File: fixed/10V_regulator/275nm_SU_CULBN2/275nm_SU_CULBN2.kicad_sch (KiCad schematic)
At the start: 18 parts, among them J1 Conn_01x04, J2 Conn_01x04, Q1 MMBT5551L, U2 LMV321, U3 AP3012

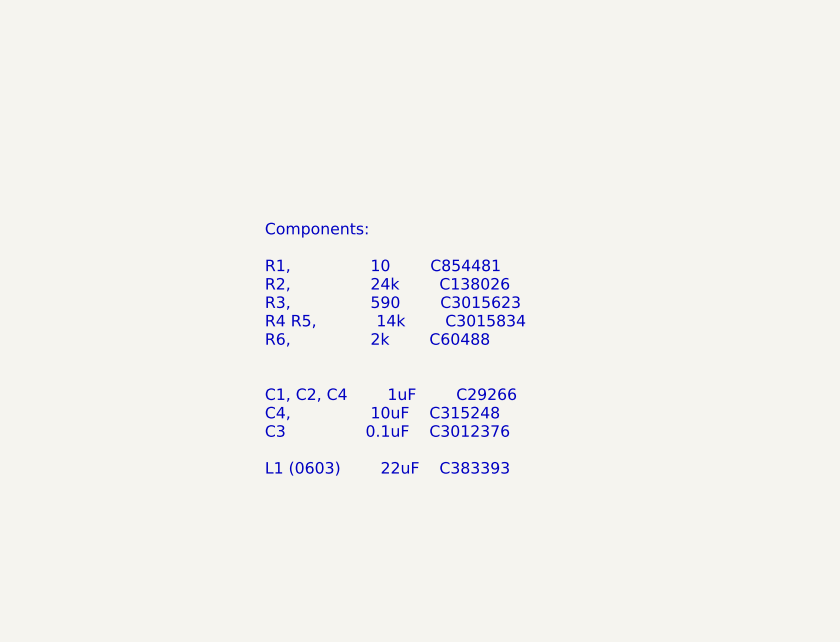
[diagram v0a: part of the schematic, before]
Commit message: Finished component selection for fixed 275nm LED.
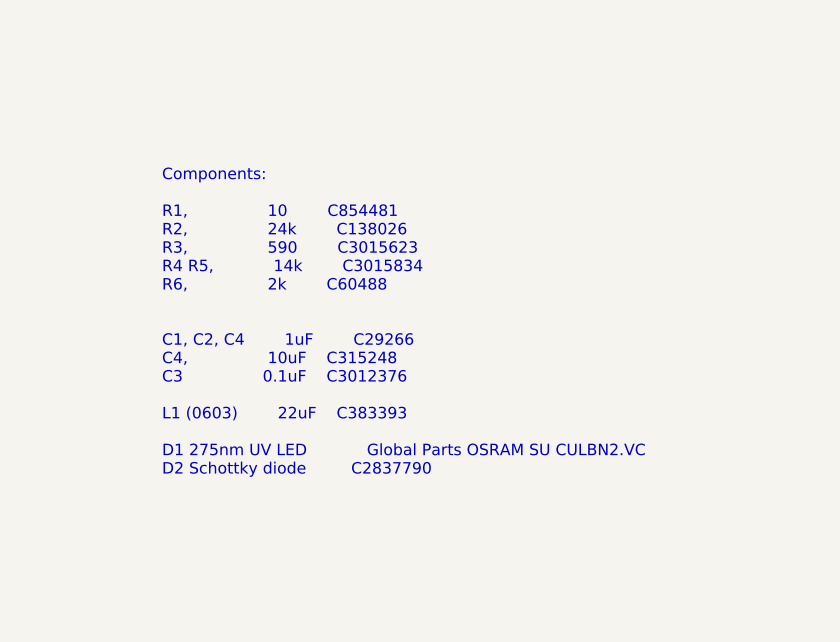
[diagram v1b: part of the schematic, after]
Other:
- note added: "Components: R1, 10 C854481 R2, 24k C138026 R3, 590 C3015623 R4 R5, 14k C3015834 R6, 2k C60488 C1, C2, C4 1uF C29266 C4, 10uF C315248 C3 0.1uF C3012376 L1 (0603) 22uF C383393 D1 275nm UV LED Global Parts OSRAM SU CULBN2.VC D2 Schottky diode C2837790"
- note removed: "Components: R1, 10 C854481 R2, 24k C138026 R3, 590 C3015623 R4 R5, 14k C3015834 R6, 2k C60488 C1, C2, C4 1uF C29266 C4, 10uF C315248 C3 0.1uF C3012376 L1 (0603) 22uF C383393"
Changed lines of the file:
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@@
     (effects (font (size 1.27 1.27)) (justify left bottom))
   )
-  (text "Components:\n\nR1,				10		C854481\nR2,				24k		C138026\nR3,				590		C3015623\nR4 R5,			14k		C3015834\nR6,				2k		C60488\n\n\nC1, C2, C4		1uF		C29266\nC4,				10uF	C315248\nC3				0.1uF	C3012376\n\nL1 (0603)		22uF	C383393\n"
-    (at 222.25 138.43 0)
+  (text "Components:\n\nR1,				10		C854481\nR2,				24k		C138026\nR3,				590		C3015623\nR4 R5,			14k		C3015834\nR6,				2k		C60488\n\n\nC1, C2, C4		1uF		C29266\nC4,				10uF	C315248\nC3				0.1uF	C3012376\n\nL1 (0603)		22uF	C383393\n\nD1 275nm UV LED			Global Parts OSRAM SU CULBN2.VC\nD2 Schottky diode 		C2837790\n"
+    (at 210.82 138.43 0)
     (effects (font (size 1.27 1.27)) (justify left bottom))
   )

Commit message: Working on 10V, fixed, 275nm LED layout.
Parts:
- D2: footprint (none) -> Diode_SMD:D_0402_1005Metric
- R4, R5, R6: footprint (none) -> Resistor_SMD:R_0402_1005Metric
- renumbered U3 to U1
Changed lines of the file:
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@@
       (effects (font (size 1.27 1.27)) (justify left))
     )
-    (property "Footprint" "" (at 103.632 35.56 90)
+    (property "Footprint" "Resistor_SMD:R_0402_1005Metric" (at 103.632 35.56 90)
       (effects (font (size 1.27 1.27)) hide)
     )
@@
       (effects (font (size 1.27 1.27)) (justify left))
     )
-    (property "Footprint" "" (at 103.632 48.26 90)
+    (property "Footprint" "Resistor_SMD:R_0402_1005Metric" (at 103.632 48.26 90)
       (effects (font (size 1.27 1.27)) hide)
     )
@@
       (effects (font (size 1.27 1.27)) (justify left))
     )
-    (property "Footprint" "" (at 41.402 34.29 90)
+    (property "Footprint" "Resistor_SMD:R_0402_1005Metric" (at 41.402 34.29 90)
       (effects (font (size 1.27 1.27)) hide)
     )
@@
   (symbol (lib_id "Regulator_Switching:AP3012") (at 71.12 39.37 0) (unit 1)
     (in_bom yes) (on_board yes) (dnp no)
-    (property "Reference" "U3" (at 64.77 33.782 0)
+    (property "Reference" "U1" (at 64.77 33.782 0)
       (effects (font (size 1.27 1.27)))
     )
@@
       (project "275nm_SU_CULBN2"
         (path "/71f5df2a-3457-4c71-8742-5c7d73c5aae8"
-          (reference "U3") (unit 1)
+          (reference "U1") (unit 1)
         )
       )
@@
       (effects (font (size 1.27 1.27)))
     )
-    (property "Footprint" "" (at 95.25 29.21 0)
-      (effects (font (size 1.27 1.27)) hide)
-    )
+    (property "Footprint" "Diode_SMD:D_0402_1005Metric" (at 95.25 29.21 0)
+      (effects (font (size 1.27 1.27)) hide)
+    )

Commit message: Worked on 275nm LED board.
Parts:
- removed D1: LED, LED_SMD:LED_0603_1608Metric, symbol Device:LED
- added D1: LED_Pad, LED_1414:LED_1414, symbol Device:LED_Pad
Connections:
- net at R1.1, U2.3 (-): now also D1.1 (K)
- net at Q1.2 (E): now also D1.2 (A)
- no-connect marks 0 -> 1
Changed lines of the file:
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@@
   (junction (at 118.11 29.21) (diameter 0) (color 0 0 0 0)
   )
+  (no_connect (at 73.66 110.998))
   (wire (pts (xy 53.34 29.21) (xy 67.31 29.21))
     (stroke (width 0) (type default))
@@
         (path "/71f5df2a-3457-4c71-8742-5c7d73c5aae8"
           (reference "J2") (unit 1)
-        )
-      )
-    )
-  )
-  (symbol (lib_id "Device:LED") (at 68.58 110.998 90) (unit 1)
-    (in_bom yes) (on_board yes) (dnp no)
-    (property "Reference" "D1" (at 71.5772 110.0074 90)
-      (effects (font (size 1.27 1.27)) (justify right))
-    )
-    (property "Value" "LED" (at 71.5772 112.3188 90)
-      (effects (font (size 1.27 1.27)) (justify right))
-    )
-    (property "Footprint" "LED_SMD:LED_0603_1608Metric" (at 68.58 110.998 0)
-      (effects (font (size 1.27 1.27)) hide)
-    )
-    (property "Datasheet" "~" (at 68.58 110.998 0)
-      (effects (font (size 1.27 1.27)) hide)
-    )
-    (pin "1")
-    (pin "2")
-    (instances
-      (project "275nm_SU_CULBN2"
-        (path "/71f5df2a-3457-4c71-8742-5c7d73c5aae8"
-          (reference "D1") (unit 1)
         )
       )
@@
         )
       )
+    )
+  )
+  (symbol (lib_id "Device:LED_Pad") (at 68.58 110.998 90) (unit 1)
+    (in_bom yes) (on_board yes) (dnp no) (fields_autoplaced)
+    (property "Reference" "D1" (at 64.77 109.728 90)
+      (effects (font (size 1.27 1.27)) (justify left))
+    )
+    (property "Value" "LED_Pad" (at 64.77 112.268 90)
+      (effects (font (size 1.27 1.27)) (justify left))
+    )
+    (property "Footprint" "LED_1414:LED_1414" (at 68.58 110.998 0)
+      (effects (font (size 1.27 1.27)) hide)
+    )
+    (property "Datasheet" "~" (at 68.58 110.998 0)
+      (effects (font (size 1.27 1.27)) hide)
+    )
+    (pin "1")
+    (pin "2")
+    (pin "3")
+    (instances
+      (project "275nm_SU_CULBN2"
+        (path "/71f5df2a-3457-4c71-8742-5c7d73c5aae8"
+          (reference "D1") (unit 1)
+        )
+      )
